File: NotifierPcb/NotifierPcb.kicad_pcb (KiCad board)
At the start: 2 copper layers, 81.6 x 97.9 mm, 32 parts, among them IC1 CD4067BEE4, IC2 ESP32-WROOM-32E__8MB_, J1 RC_433_MHZ_RF, J2 UART_Conn, J3 Power_Conn, J5 Vcc, J6 Vcc, U1 HT75xx-1-SOT89

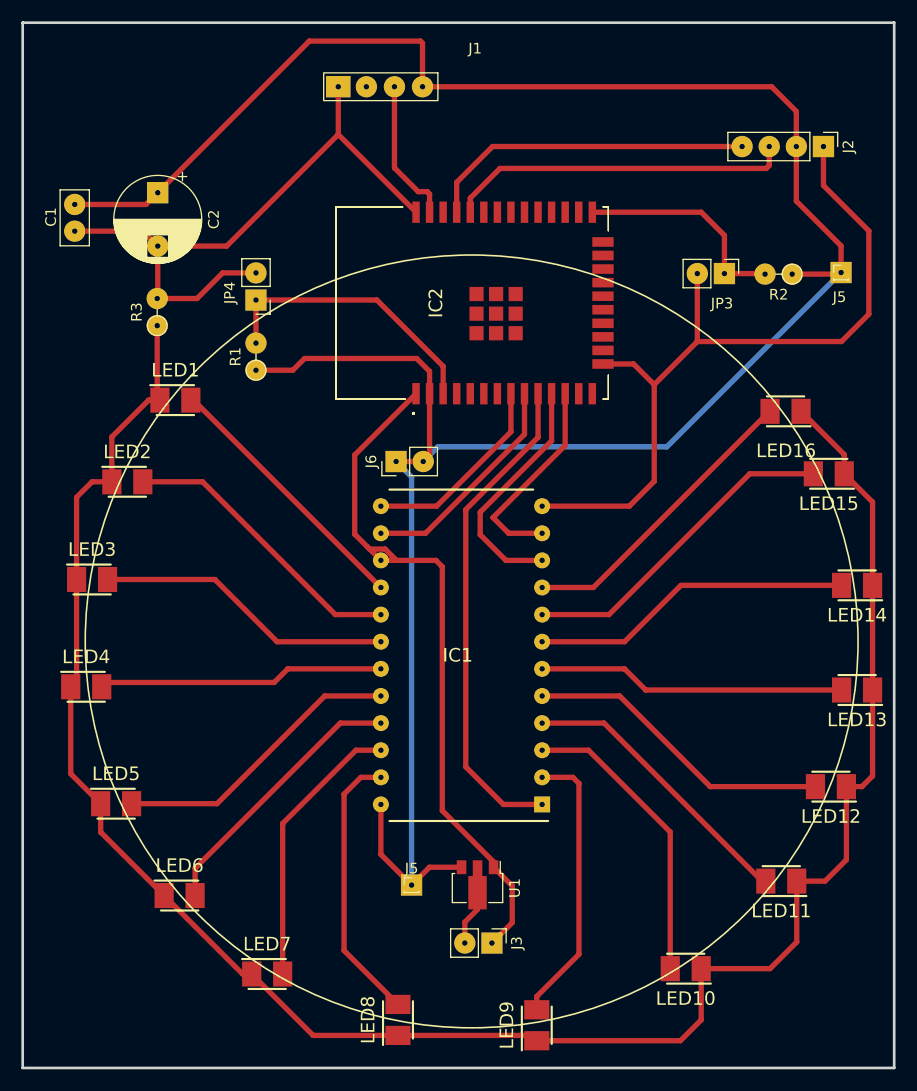
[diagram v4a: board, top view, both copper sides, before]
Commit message: power rf receiver with 5V
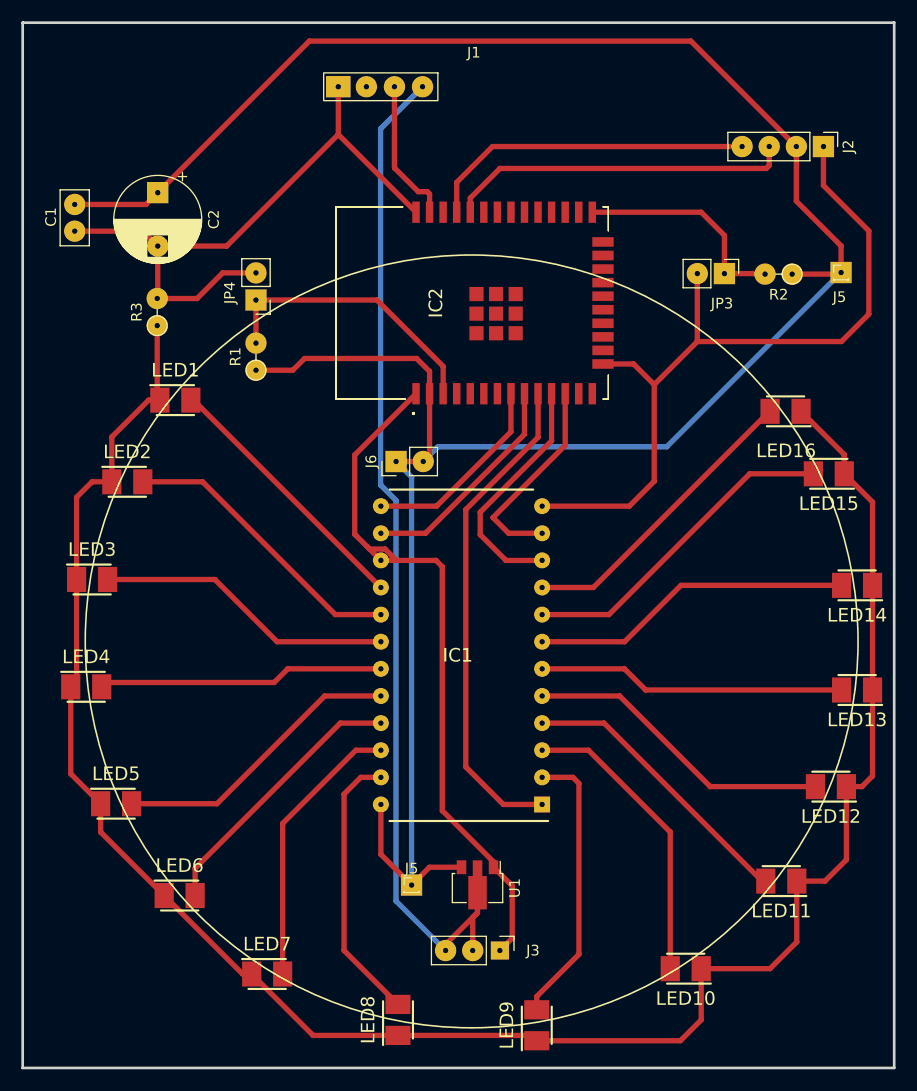
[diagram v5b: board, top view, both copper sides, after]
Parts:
- J3: value Power_Conn -> Power; footprint Connector_PinHeader_2.54mm:PinHeader_1x02_P2.54mm_Vertical -> Connector_PinHeader_2.54mm:PinHeader_1x03_P2.54mm_Vertical
- moved J3 1.02 mm to (143.6, 124.7)
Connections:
- J1 pad 1: +3.3V -> +5V
- J3 pad 2: POWER -> +5V
- R1 pad 1: VCC -> +3.3V
- U1 pad 2: POWER -> +5V
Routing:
- net +5V: track 0.00 -> 97.6 mm
- net POWER: track 7.51 -> 0.00 mm
- net +3.3V: track 229.9 -> 225.6 mm
